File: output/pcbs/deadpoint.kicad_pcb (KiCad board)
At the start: 2 copper layers, 152.8 x 120 mm, 75 parts, among them J1 Jumper

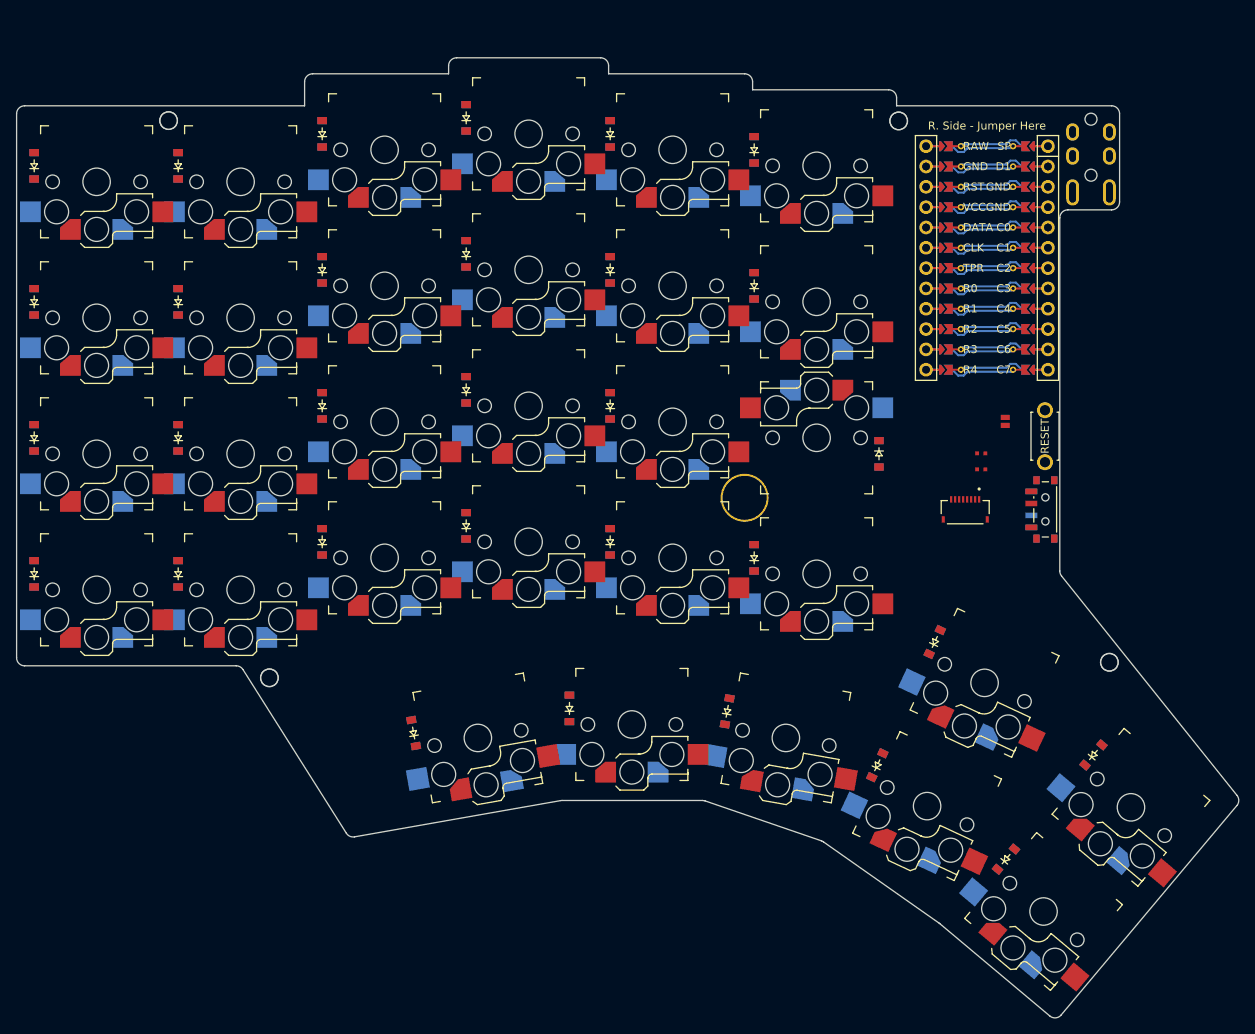
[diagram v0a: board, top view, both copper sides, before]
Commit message: new layout. added pinky splay and increased thumb splay
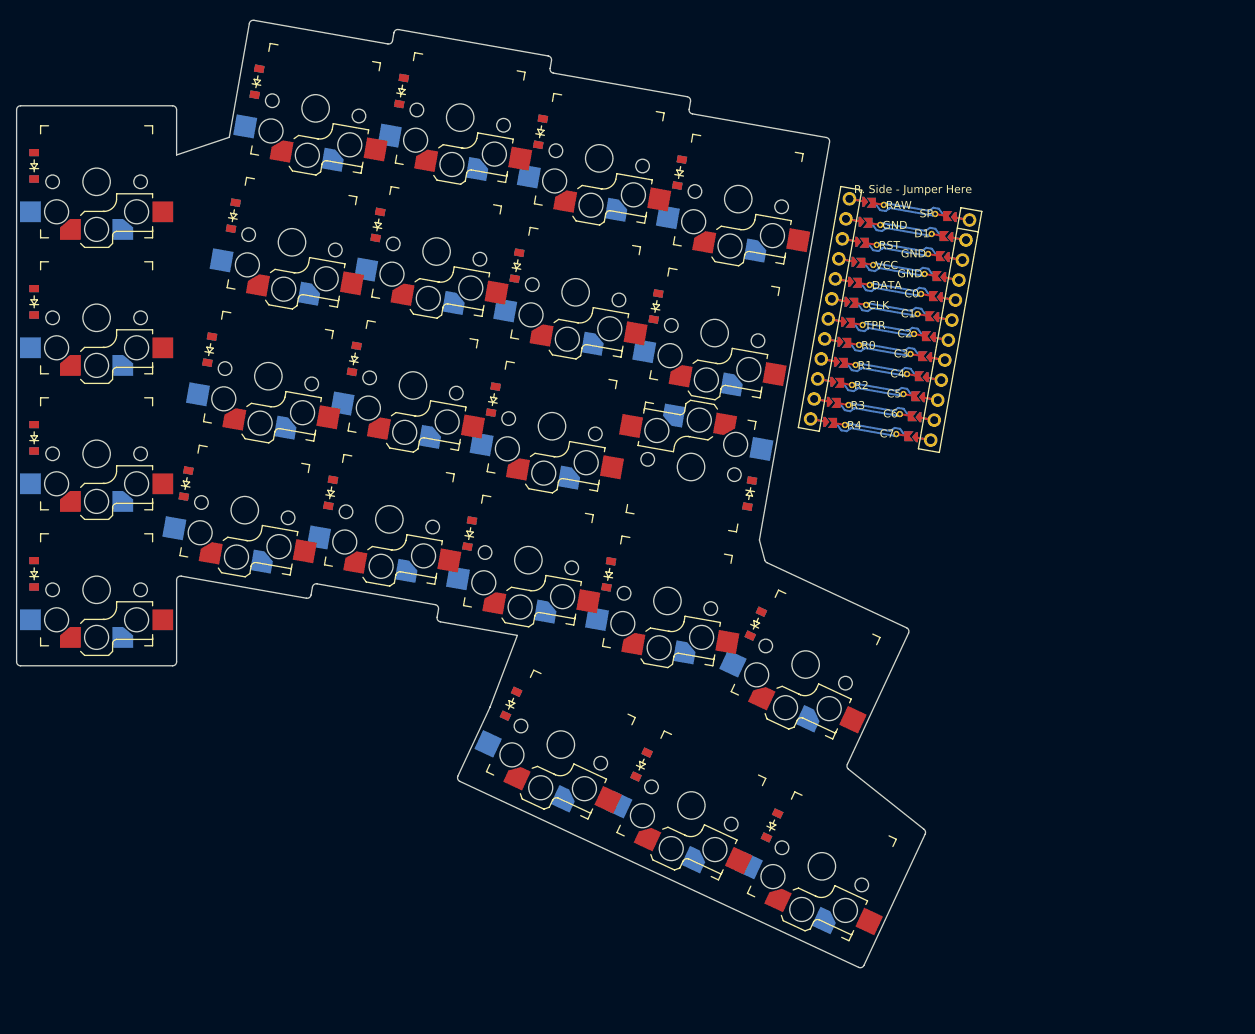
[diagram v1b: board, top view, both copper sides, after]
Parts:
- removed B1: , kbd:ResetSW
- removed D25, D26, D27, D28, D29, D30, D31: , ComboDiode
- removed DISP1: HRS_FH34SRJ-8S-0.5SH_50_, HRS_FH34SRJ-8S-0.5SH_50_
- removed DISP2, DISP3: RES_ERJ2RKF4701X, RES_ERJ2RKF4701X
- removed H1, H2, H3, H4: , Screw_Hole
- removed J1: Jumper, lib:Jumper
- removed S25, S26, S27, S28, S29, S30, S31: , PG1350
- removed SW1: , power_switch
- removed TP1: , trackpoint_mount_t430
- removed TRRS1: TRRS-PJ-320A-dual, ceoloide:TRRS-PJ-320A-dual (reversible, symmetric)
- moved S24 87.6 mm to (190.7, 134.6), turned to 155 degrees
- moved D24 84.5 mm to (184.4, 129.5), turned to 65 degrees
- moved D22 48.9 mm to (168.1, 121.8), turned to 65 degrees
- moved S22 48.6 mm to (174.3, 127.0), turned to 155 degrees
- moved S23 45.4 mm to (188.6, 109.3), turned to 155 degrees
- moved D23 42.2 mm to (182.4, 104.2), turned to 65 degrees
- moved S21 38.4 mm to (158.0, 119.4), turned to 155 degrees
- moved D21 35.4 mm to (151.8, 114.2), turned to 65 degrees
- moved D18 20.6 mm to (181.6, 88.0), turned to 260 degrees
- moved D8 14.4 mm to (120.0, 36.5), turned to 80 degrees
- moved MCU1 14.2 mm to (199.4, 65.0), turned to -10 degrees
- moved S8 13.1 mm to (127.4, 39.8), turned to 170 degrees
- moved D7 12.8 mm to (117.1, 53.2), turned to 80 degrees
- moved D6 11.7 mm to (114.1, 70.0), turned to 80 degrees
- moved S7 11.4 mm to (124.4, 56.6), turned to 170 degrees
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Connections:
- D1 pad 2: pinky2_bottom -> pinky_bottom
- D10 pad 2: ring_home -> middle_home
- D11 pad 2: ring_top -> middle_top
- D12 pad 2: ring_num -> middle_num
- D13 pad 2: middle_bottom -> index_bottom
- D14 pad 2: middle_home -> index_home
- D15 pad 2: middle_top -> index_top
- D16 pad 2: middle_num -> index_num
- D17 pad 2: index_bottom -> inner_bottom
- D18 pad 2: index_home -> inner_home
- D19 pad 2: index_top -> inner_top
- D2 pad 2: pinky2_home -> pinky_home
- D20 pad 2: index_num -> inner_num
- D21 pad 1: R3 -> R4
- D21 pad 2: inner_bottom -> flexion_lower
- D22 pad 1: R2 -> R4
- D22 pad 2: inner_home -> base_lower
- D23 pad 1: R1 -> R3
- D23 pad 2: inner_top -> base_upper
- D24 pad 1: R0 -> R4
- D24 pad 2: inner_num -> extension_lower
- D3 pad 2: pinky2_top -> pinky_top
- D4 pad 2: pinky2_num -> pinky_num
- D5 pad 2: pinky_bottom -> ring_bottom
- D6 pad 2: pinky_home -> ring_home
- D7 pad 2: pinky_top -> ring_top
- D8 pad 2: pinky_num -> ring_num
- D9 pad 2: ring_bottom -> middle_bottom
- S1 pad 1: C0 -> C1
- S1 pad 2: pinky2_bottom -> pinky_bottom
- S10 pad 1: C2 -> C3
- S10 pad 2: ring_home -> middle_home
- S11 pad 1: C2 -> C3
- S11 pad 2: ring_top -> middle_top
- S12 pad 1: C2 -> C3
- S12 pad 2: ring_num -> middle_num
- S13 pad 1: C3 -> C4
- S13 pad 2: middle_bottom -> index_bottom
- S14 pad 1: C3 -> C4
- S14 pad 2: middle_home -> index_home
- S15 pad 1: C3 -> C4
- S15 pad 2: middle_top -> index_top
- S16 pad 1: C3 -> C4
- S16 pad 2: middle_num -> index_num
- S17 pad 1: C4 -> C5
- S17 pad 2: index_bottom -> inner_bottom
- S18 pad 1: C4 -> C5
- S18 pad 2: index_home -> inner_home
- S19 pad 1: C4 -> C5
- S19 pad 2: index_top -> inner_top
- S2 pad 1: C0 -> C1
- S2 pad 2: pinky2_home -> pinky_home
- S20 pad 1: C4 -> C5
- S20 pad 2: index_num -> inner_num
- S21 pad 1: C5 -> C4
- S21 pad 2: inner_bottom -> flexion_lower
- S22 pad 2: inner_home -> base_lower
- S23 pad 2: inner_top -> base_upper
- S24 pad 1: C5 -> C6
- S24 pad 2: inner_num -> extension_lower
- S3 pad 1: C0 -> C1
- S3 pad 2: pinky2_top -> pinky_top
- S4 pad 1: C0 -> C1
- S4 pad 2: pinky2_num -> pinky_num
- S5 pad 1: C1 -> C2
- S5 pad 2: pinky_bottom -> ring_bottom
- S6 pad 1: C1 -> C2
- S6 pad 2: pinky_home -> ring_home
- S7 pad 1: C1 -> C2
- S7 pad 2: pinky_top -> ring_top
- S8 pad 1: C1 -> C2
- S8 pad 2: pinky_num -> ring_num
- S9 pad 1: C2 -> C3
- S9 pad 2: ring_bottom -> middle_bottom
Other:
- board size 152.8 x 120 mm -> 113.6 x 118.4 mm

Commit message: adjust splay
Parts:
- moved D8 4.93 mm to (115.1, 36.5), turned to 85 degrees
- moved S8 4.71 mm to (122.7, 39.2), turned to 175 degrees
- moved D7 3.47 mm to (113.6, 53.5), turned to 85 degrees
- moved S7 3.23 mm to (121.2, 56.1), turned to 175 degrees
- moved D6 2.04 mm to (112.1, 70.4), turned to 85 degrees
- moved D23 1.95 mm to (181.7, 102.4)
- moved S23 1.95 mm to (187.9, 107.5)
- moved S6 1.74 mm to (119.7, 73.1), turned to 175 degrees
- moved D13 1.63 mm to (146.4, 91.4)
- moved D14 1.63 mm to (149.4, 74.6)
- moved D15 1.63 mm to (152.3, 57.9)
- moved D16 1.63 mm to (155.3, 41.1)
- moved S13 1.63 mm to (153.7, 94.7)
- moved S14 1.63 mm to (156.7, 77.9)
- moved S15 1.63 mm to (159.7, 61.2)
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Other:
- board size 113.6 x 118.4 mm -> 113.4 x 117.3 mm
